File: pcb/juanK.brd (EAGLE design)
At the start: 155.9 x 110.5 mm, 83 parts, among them IC1 MEGA8-P, IC2 7805TV, T1 2N3904, T2 TIC106S, T3 TIC106S, T4 TIC106S, T5 TIC106S, T6 TIC106S, T7 TIC106S

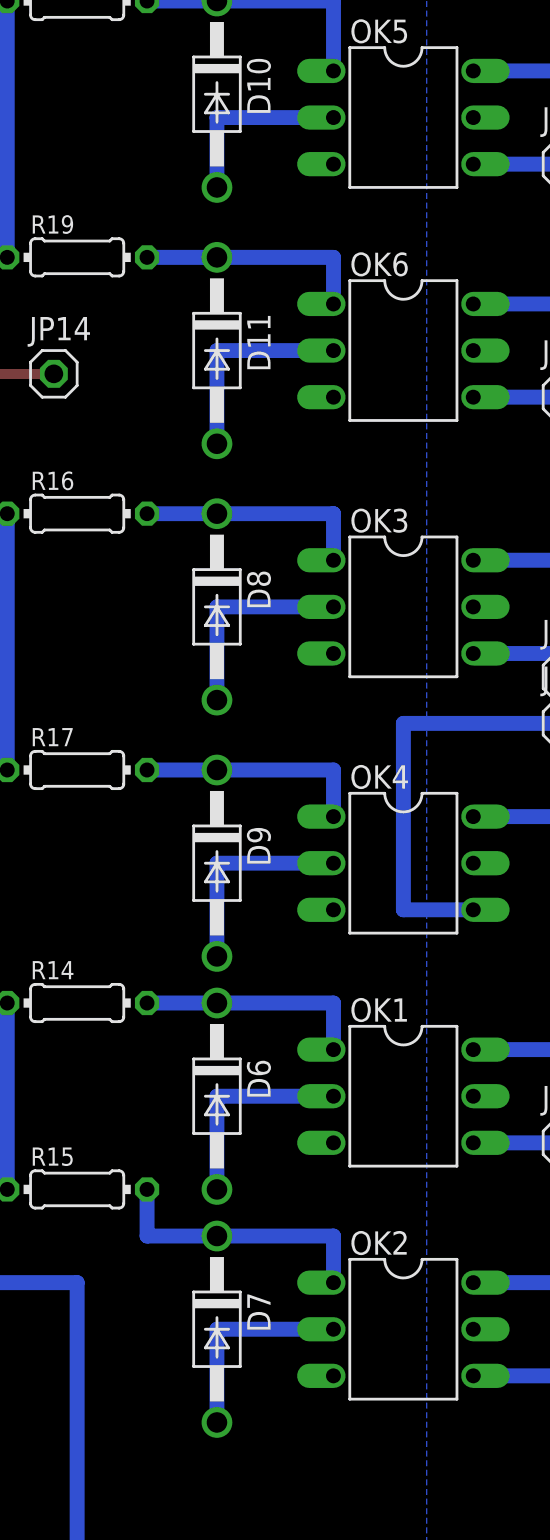
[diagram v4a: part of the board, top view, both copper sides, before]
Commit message: Corregir conexión de tierra en los MOC
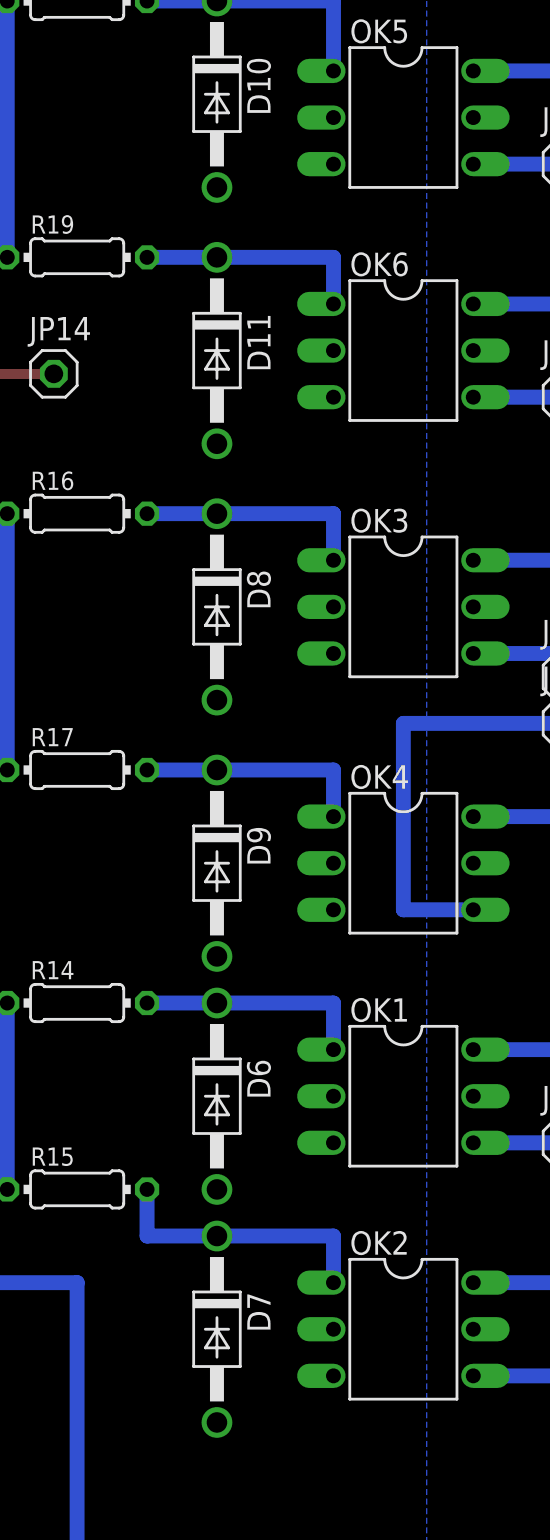
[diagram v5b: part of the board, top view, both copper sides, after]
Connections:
- removed net N$29: D6.A, OK1.2
- removed net N$31: D7.A, OK2.2
- removed net N$33: D8.A, OK3.2
- removed net N$34: D9.A, OK4.2
- removed net N$38: D11.A, OK6.2
- removed net N$39: D10.A, OK5.2
- net GND: now also D10.A, D11.A, D6.A, D7.A, D8.A, D9.A, OK1.2, OK2.2, OK3.2, OK4.2, OK5.2, OK6.2
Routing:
- net N$38: track 11.4 -> 0.00 mm
- net N$34: track 11.4 -> 0.00 mm
- net N$33: track 11.4 -> 0.00 mm
- net N$31: track 11.4 -> 0.00 mm
- net N$29: track 11.4 -> 0.00 mm
- net N$39: track 10.2 -> 0.00 mm
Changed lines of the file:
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@@
 <contactref element="R2" pad="1"/>
 <contactref element="LED1" pad="K"/>
+<contactref element="D10" pad="A"/>
+<contactref element="OK5" pad="2"/>
+<contactref element="D11" pad="A"/>
+<contactref element="OK6" pad="2"/>
+<contactref element="D9" pad="A"/>
+<contactref element="OK4" pad="2"/>
+<contactref element="D8" pad="A"/>
+<contactref element="OK3" pad="2"/>
+<contactref element="D6" pad="A"/>
+<contactref element="OK1" pad="2"/>
+<contactref element="D7" pad="A"/>
+<contactref element="OK2" pad="2"/>
 </signal>
 <signal name="N$14">
@@
 <wire x1="71.12" y1="41.91" x2="71.12" y2="39.37" width="0.8128" layer="16"/>
 </signal>
-<signal name="N$29">
-<contactref element="D6" pad="A"/>
-<contactref element="OK1" pad="2"/>
-<wire x1="71.12" y1="36.83" x2="64.77" y2="36.83" width="0.8128" layer="16"/>
-<wire x1="64.77" y1="36.83" x2="64.77" y2="31.75" width="0.8128" layer="16"/>
-</signal>
 <signal name="N$30">
 <contactref element="R15" pad="2"/>
@@
 <wire x1="64.77" y1="29.21" x2="71.12" y2="29.21" width="0.8128" layer="16"/>
 <wire x1="71.12" y1="29.21" x2="71.12" y2="26.67" width="0.8128" layer="16"/>
-</signal>
-<signal name="N$31">
-<contactref element="D7" pad="A"/>
-<contactref element="OK2" pad="2"/>
-<wire x1="71.12" y1="24.13" x2="64.77" y2="24.13" width="0.8128" layer="16"/>
-<wire x1="64.77" y1="24.13" x2="64.77" y2="19.05" width="0.8128" layer="16"/>
 </signal>
 <signal name="N$32">
@@
 <wire x1="71.12" y1="68.58" x2="71.12" y2="66.04" width="0.8128" layer="16"/>
 </signal>
-<signal name="N$33">
-<contactref element="D8" pad="A"/>
-<contactref element="OK3" pad="2"/>
-<wire x1="71.12" y1="63.5" x2="64.77" y2="63.5" width="0.8128" layer="16"/>
-<wire x1="64.77" y1="63.5" x2="64.77" y2="58.42" width="0.8128" layer="16"/>
-</signal>
-<signal name="N$34">
-<contactref element="D9" pad="A"/>
-<contactref element="OK4" pad="2"/>
-<wire x1="64.77" y1="44.45" x2="64.77" y2="49.53" width="0.8128" layer="16"/>
-<wire x1="64.77" y1="49.53" x2="71.12" y2="49.53" width="0.8128" layer="16"/>
-</signal>
 <signal name="N$35">
 <contactref element="R17" pad="2"/>
@@
 <wire x1="71.12" y1="82.55" x2="71.12" y2="80.01" width="0.8128" layer="16"/>
 </signal>
-<signal name="N$38">
-<contactref element="D11" pad="A"/>
-<contactref element="OK6" pad="2"/>
-<wire x1="71.12" y1="77.47" x2="64.77" y2="77.47" width="0.8128" layer="16"/>
-<wire x1="64.77" y1="77.47" x2="64.77" y2="72.39" width="0.8128" layer="16"/>
-</signal>
-<signal name="N$39">
-<contactref element="D10" pad="A"/>
-<contactref element="OK5" pad="2"/>
-<wire x1="71.12" y1="90.17" x2="64.77" y2="90.17" width="0.8128" layer="16"/>
-<wire x1="64.77" y1="90.17" x2="64.77" y2="86.36" width="0.8128" layer="16"/>
-</signal>
 <signal name="GND1">
